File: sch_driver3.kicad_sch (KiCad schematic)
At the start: 20 parts, among them Q3 PSMN4R0-30YLDX, U13 TS5A3159ADCK, U2 ADA4099-2xR, U23 OPA365AIDBV, U5 ADA4099-1

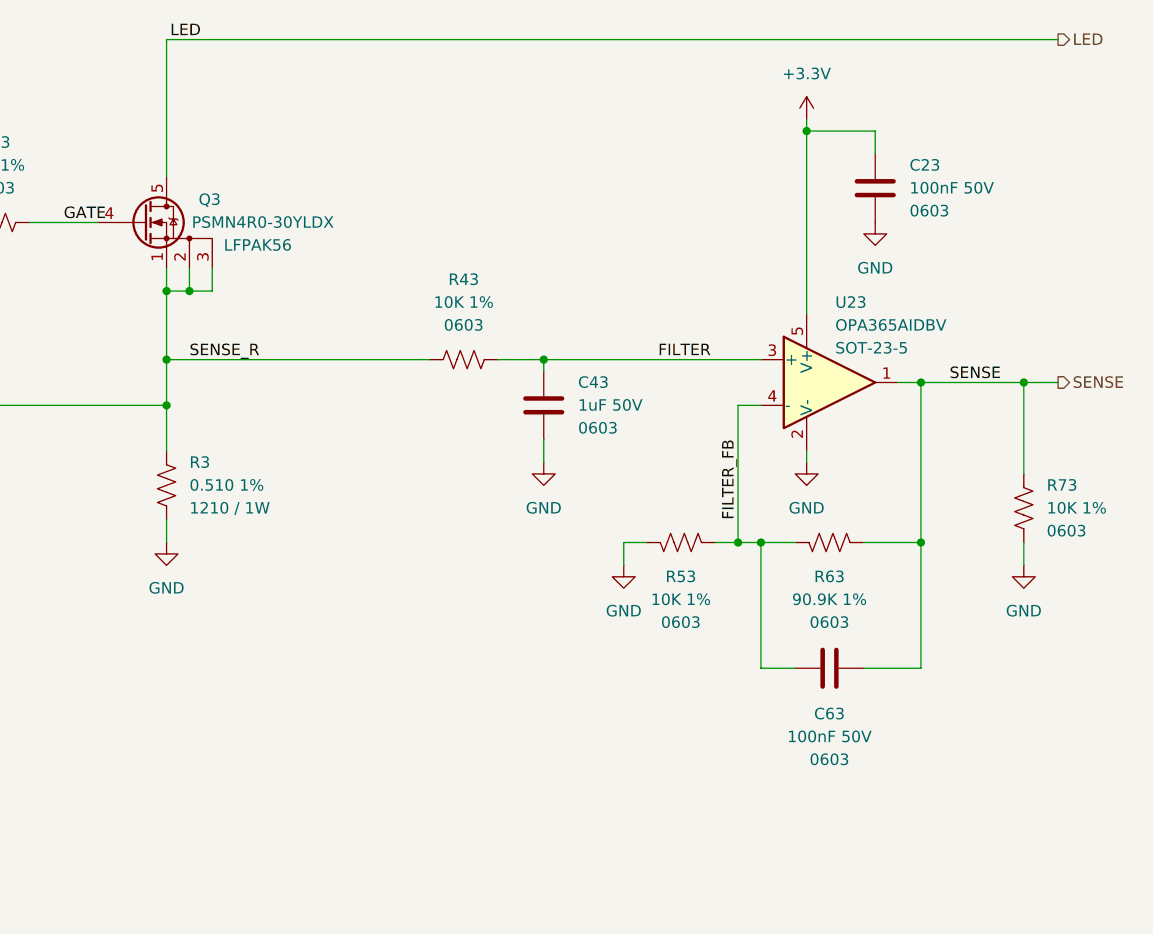
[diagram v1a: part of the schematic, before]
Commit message: Initial placement on 45 x 30 mm outline. Dropped sense apms. Switch to two 2x6 connectors.
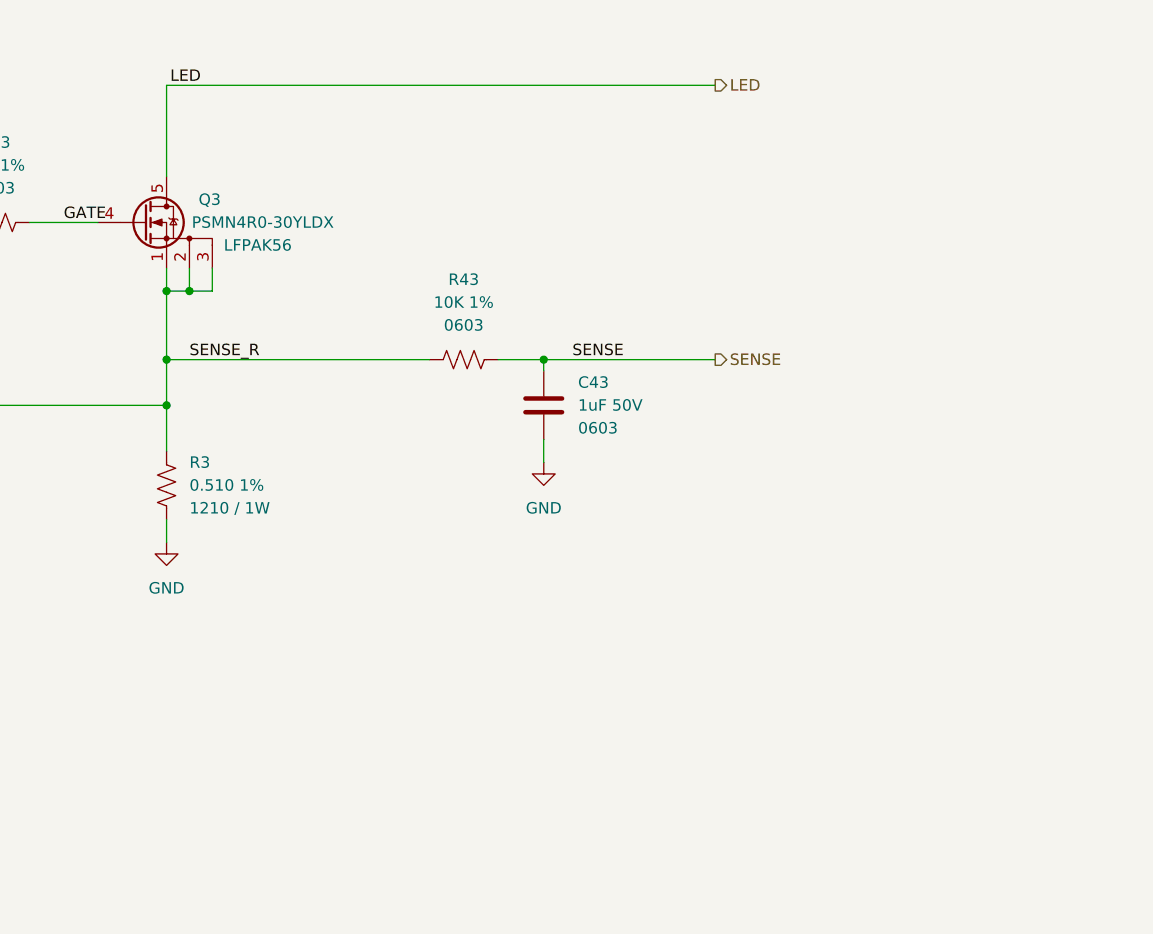
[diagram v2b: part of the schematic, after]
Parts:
- removed C23, C63: 100nF 50V, $Local:C_0603_1608Metric, symbol $Local:C_0603_100NF_50V
- removed R53, R73: 10K 1%, $Local:R_0603_1608Metric, symbol $Local:R_0603_10K
- removed R63: 90.9K 1%, $Local:R_0603_1608Metric, symbol $Local:R_0603_10K
- removed U23: OPA365AIDBV, $Local:SOT-23-5, symbol $Local:OPA365AIDBV
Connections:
- net FILTER is gone; now on net SENSE: C43.1, R43.1
